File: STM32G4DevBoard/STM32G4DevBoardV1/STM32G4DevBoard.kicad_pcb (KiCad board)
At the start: 4 copper layers, 44.7 x 23.5 mm, 26 parts, among them J1 USB_B_Micro, J2 Conn_01x13, J3 Conn_01x13, U1 STM32G431KBTx, U2 LD3985M33R_SOT23, Y1 24MHz

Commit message: Finished Crystal Layout
Made changes for crystal layout
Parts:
- C180, C3: moved to F.Cu
- moved C1 31.1 mm to (112.4, 98.0), turned to 180 degrees
- moved R1 10.6 mm to (143.3, 98.2), turned to 180 degrees
- moved C180 5.99 mm to (139.2, 94.7), turned to 270 degrees
- moved C3 4.33 mm to (139.2, 91.2), turned to 270 degrees
- moved C7 3.23 mm to (136.7, 95.1)
- moved C4 3.07 mm to (131.3, 87.1)
- moved C5 2.87 mm to (131.3, 85.3)
- moved FB1 1.75 mm to (127.8, 85.3), turned to 0 degrees
- moved Y1 1.27 mm to (142.2, 93.2)
- moved RST_SW1 0.92 mm to (112.0, 98.0)
- moved C11 0.51 mm to (122.4, 91.8)
- moved C6 0.51 mm to (124.4, 91.8)
- moved C8 0.51 mm to (126.3, 91.8)
- moved C10 0.25 mm to (116.6, 91.6)
- moved C12 0.25 mm to (118.7, 95.8)
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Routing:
- net GND: track 0.00 -> 38.3 mm, vias 0 -> 15
- net OSC_IN: track 0.00 -> 8.04 mm
- net OSC_OUT: track 0.00 -> 4.94 mm

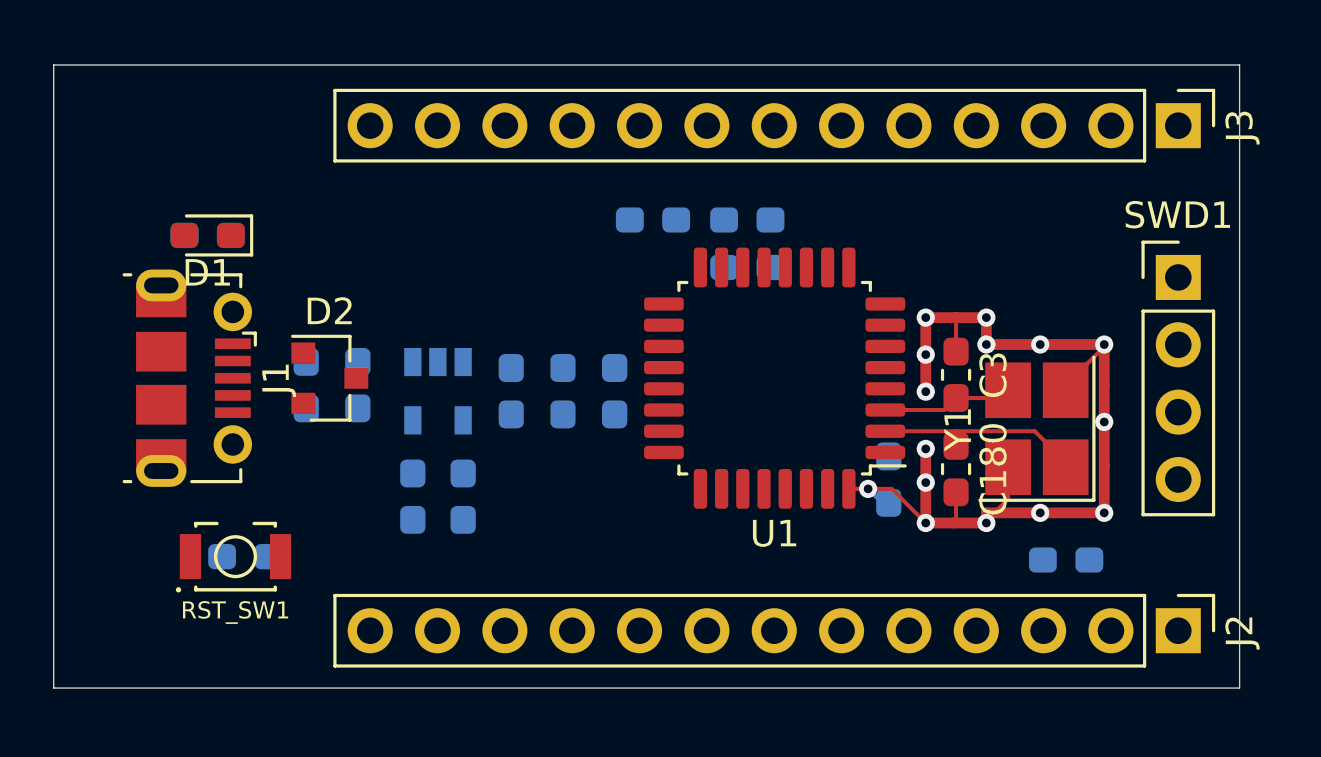
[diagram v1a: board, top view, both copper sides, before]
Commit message: Made plenty of Progress, finish routing power and a couple of pins
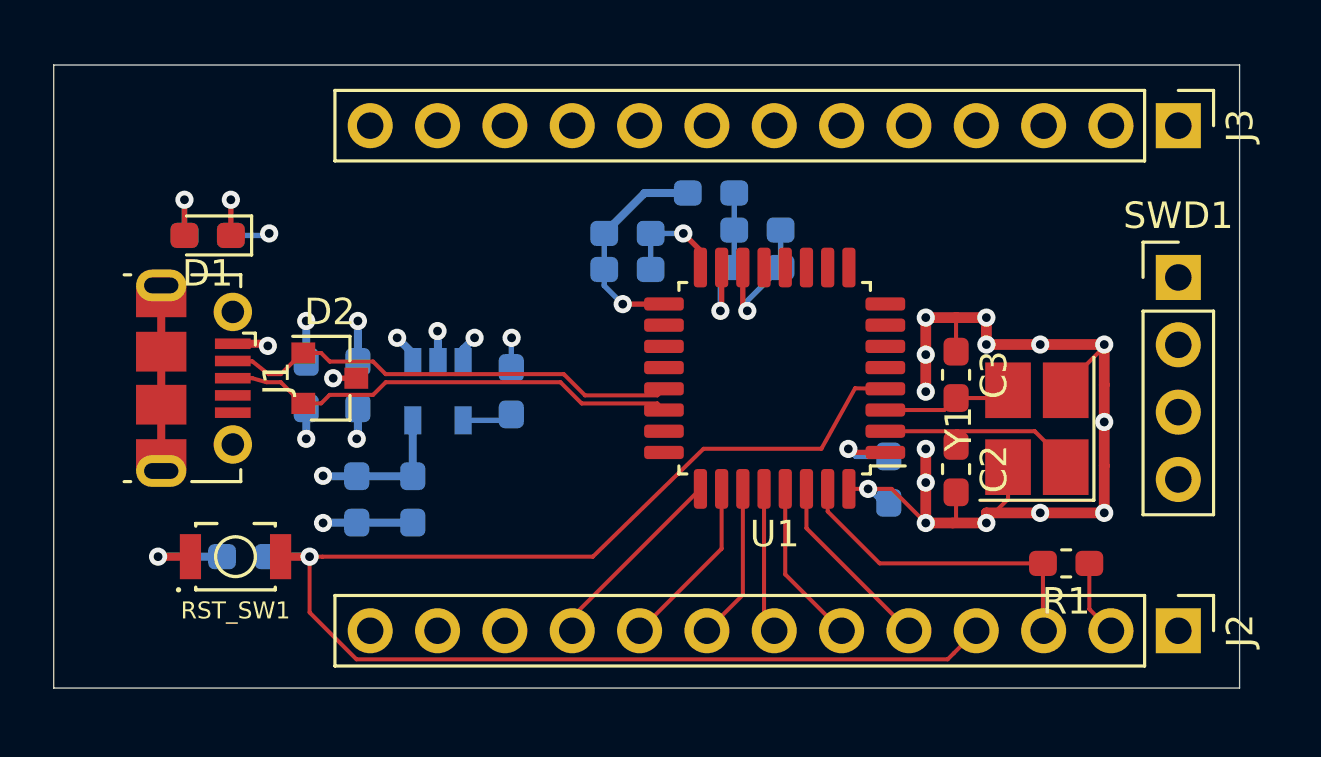
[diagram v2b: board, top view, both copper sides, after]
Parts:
- R1: moved to F.Cu
- moved C6 6.43 mm to (126.8, 85.9), turned to 180 degrees
- moved C8 4.62 mm to (126.8, 87.2), turned to 180 degrees
- moved C13 4.02 mm to (116.6, 95.9)
- moved FB1 2.41 mm to (129.9, 84.3)
- moved C5 0.54 mm to (131.7, 85.7)
- moved C4 0.38 mm to (131.7, 87.1)
- moved R1 0.13 mm to (143.3, 98.3)
- moved C12 0.10 mm to (118.7, 95.9)
- renumbered C180 to C2
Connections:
- C8 pad 1: 3.3V_VDD -> GND
- C8 pad 2: GND -> 3.3V_VDD
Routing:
- net NRST: track 0.00 -> 55.8 mm, vias 0 -> 1
- net GND: track 38.3 -> 71.0 mm, vias 15 -> 25
- net USB_D-: track 0.00 -> 17.5 mm
- net USB_D+: track 0.00 -> 17.4 mm
- net 3.3V_VDD: track 0.00 -> 16.8 mm, vias 0 -> 3
- net BOOT0: track 0.00 -> 12.3 mm
- net 5V_USB: track 0.00 -> 8.19 mm, vias 0 -> 6
- net PA15: track 0.00 -> 7.35 mm
- net PB7: track 0.00 -> 6.95 mm
- net PB3: track 0.00 -> 6.63 mm
- net 3.3V_VDDA: track 0.00 -> 6.32 mm, vias 0 -> 1
- net PB6: track 0.00 -> 6.23 mm
- net PB4: track 0.00 -> 5.91 mm
- net PB5: track 0.00 -> 5.51 mm
- net Net-(D1-Pad2): track 0.00 -> 2.99 mm, vias 0 -> 1
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- added copper zone on PWR, net 5V_USB

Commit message: Finish Power splitting and pin routing
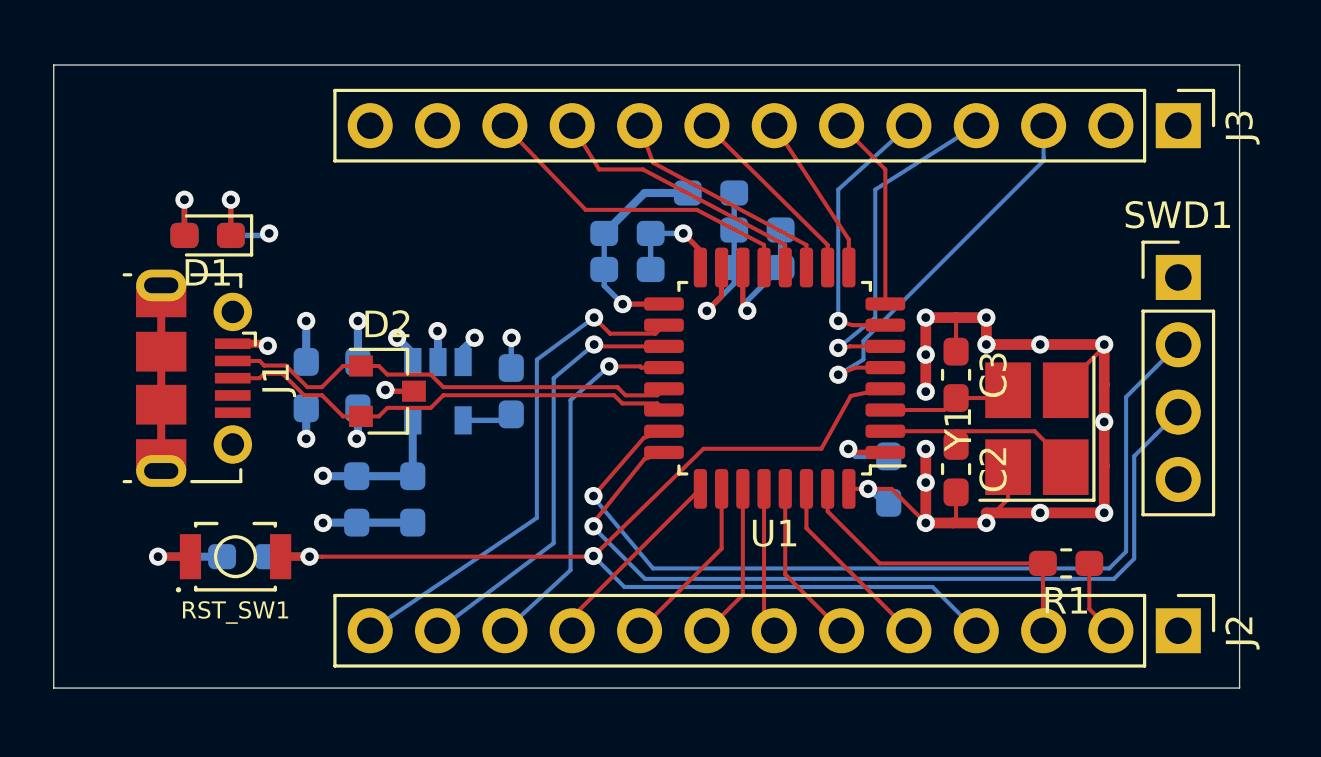
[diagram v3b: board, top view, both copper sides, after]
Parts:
- moved D2 2.23 mm to (117.7, 91.8)
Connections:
- net SWCLK renamed SWCLK_P
- net SWDIO renamed SWDIO_M
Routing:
- net SWDIO_M: track 0.00 -> 34.0 mm, vias 0 -> 1
- net SWCLK_P: track 0.00 -> 31.8 mm, vias 0 -> 1
- net PA8: track 0.00 -> 19.3 mm, vias 0 -> 1
- net PA9: track 0.00 -> 16.4 mm, vias 0 -> 1
- net Net-(J3-Pad3): track 0.00 -> 14.6 mm, vias 0 -> 1
- net PA10: track 0.00 -> 13.8 mm, vias 0 -> 1
- net NRST: track 55.8 -> 42.8 mm, vias 1 -> 2
- net Net-(J3-Pad4): track 0.00 -> 12.9 mm, vias 0 -> 1
- net SWO: track 0.00 -> 12.3 mm
- net Net-(J3-Pad10): track 0.00 -> 10.5 mm
- net Net-(J3-Pad5): track 0.00 -> 10.3 mm, vias 0 -> 1
- net Net-(J3-Pad9): track 0.00 -> 8.90 mm
- net Net-(J3-Pad6): track 0.00 -> 7.41 mm
- net Net-(J3-Pad8): track 0.00 -> 7.25 mm
- net Net-(J3-Pad7): track 0.00 -> 6.19 mm
- added copper zone on PWR, net 3.3V_VDDA

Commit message: Completed splitting ground plane and board routing
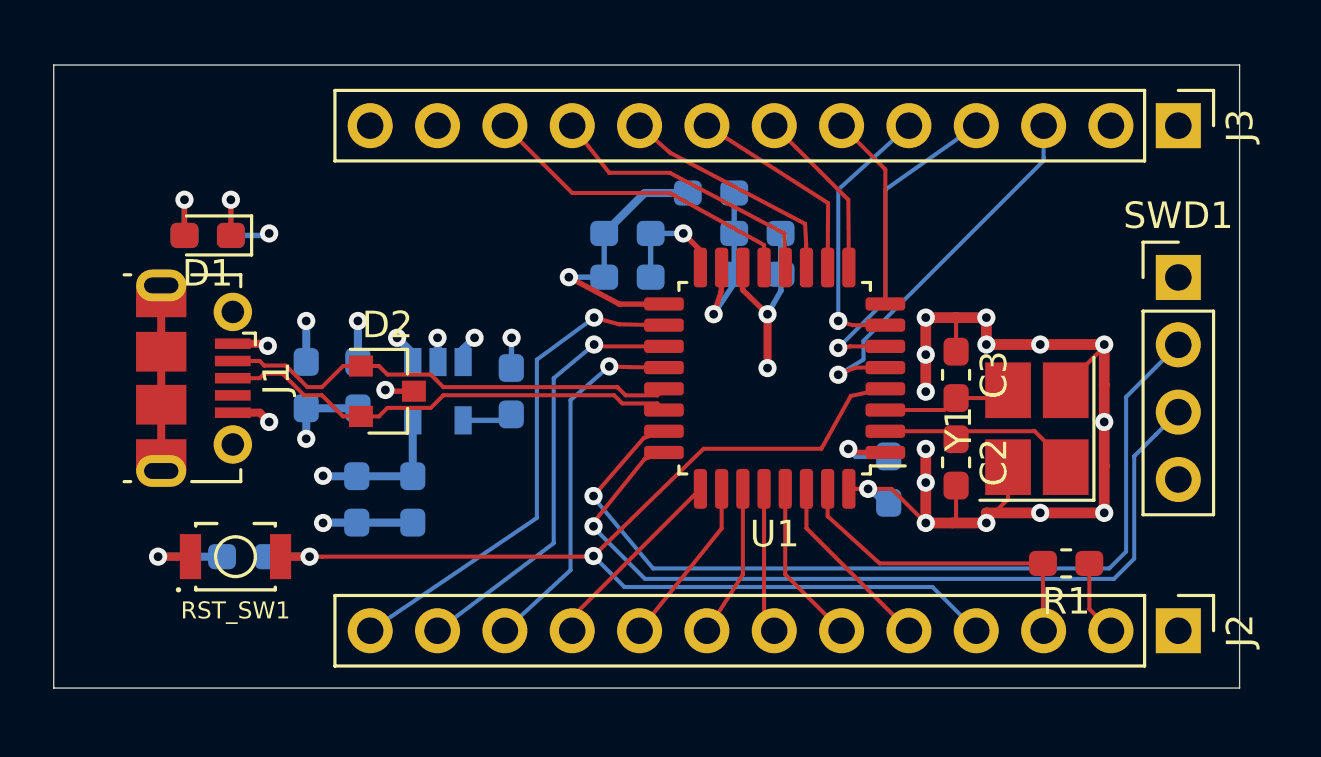
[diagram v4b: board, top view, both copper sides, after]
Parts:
- moved C8 0.29 mm to (126.8, 87.5)
- moved C2 0.25 mm to (139.2, 94.5)
- moved C4 0.25 mm to (131.7, 87.4)
- moved C5 0.13 mm to (131.7, 85.9)
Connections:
- net SWCLK_P renamed SWCLK
- net SWDIO_M renamed SWDIO
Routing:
- net GND: track 71.2 -> 75.8 mm, vias 25 -> 26
- net 3.3V_VDD: track 16.8 -> 19.1 mm
- net Net-(J3-Pad8): track 7.25 -> 7.85 mm

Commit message: Updated Silkscreen label for pins
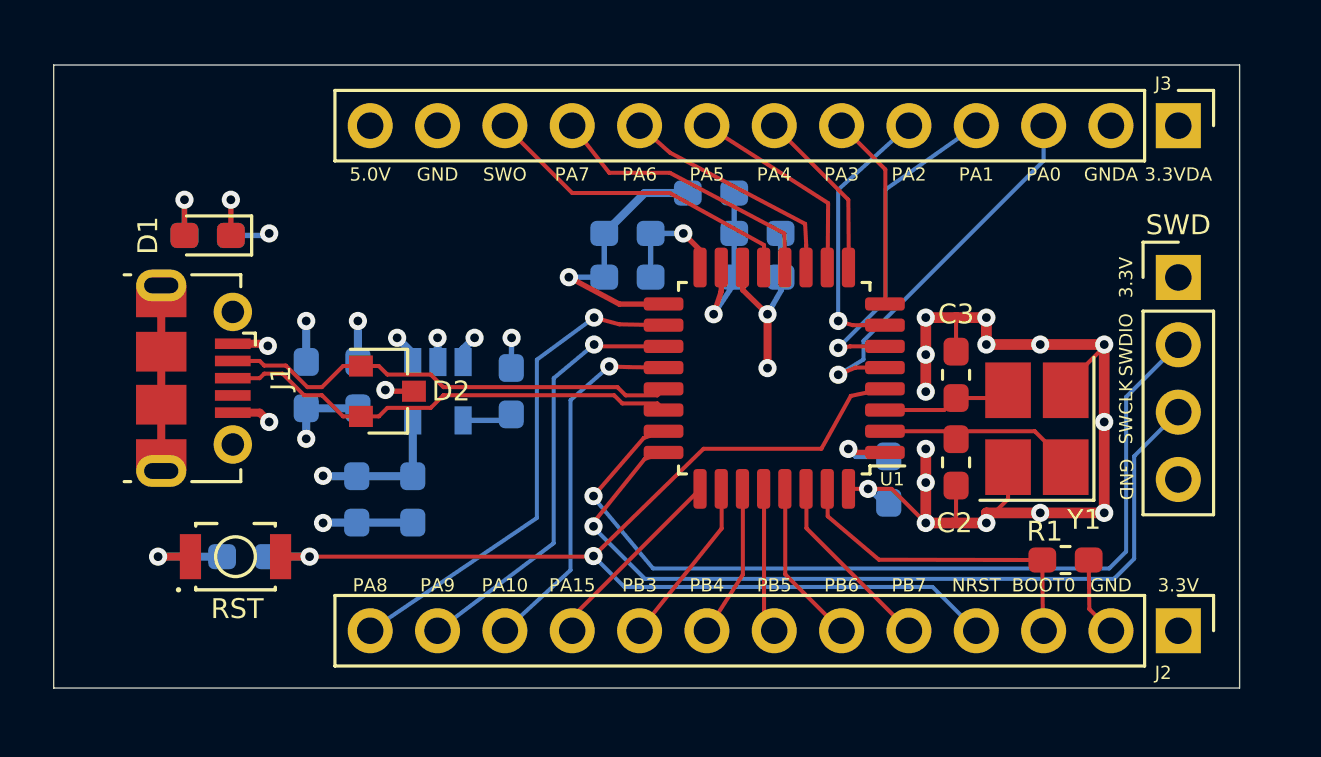
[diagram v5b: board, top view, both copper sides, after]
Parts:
- moved R1 0.13 mm to (143.3, 98.2)
- moved C4 0.11 mm to (131.7, 87.5)
- renumbered RST_SW1 to RST, SWD1 to SWD
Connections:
- net Net-(J3-Pad10) renamed PA7
- net Net-(J3-Pad3) renamed PA0
- net Net-(J3-Pad4) renamed PA1
- net Net-(J3-Pad5) renamed PA2
- net Net-(J3-Pad6) renamed PA3
- net Net-(J3-Pad7) renamed PA4
- net Net-(J3-Pad8) renamed PA5
- net Net-(J3-Pad9) renamed PA6
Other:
- board text added: "3.3V"
- board text added: "3.3VDA"
- board text added: "5.0V"
- board text added: "BG STM32 BRK V1.00"
- board text added: "BOOT0"
- board text added: "GND"
- board text added: "GNDA"
- board text added: "NRST"
- board text added: "PA0"
- board text added: "PA1"
- board text added: "PA10"
- board text added: "PA15"
- board text added: "PA2"
- board text added: "PA3"
- board text added: "PA4"
- board text added: "PA5"
- board text added: "PA6"
- board text added: "PA7"
- board text added: "PA8"
- board text added: "PA9"
- board text added: "PB3"
- board text added: "PB4"
- board text added: "PB5"
- board text added: "PB6"
- board text added: "PB7"
- board text added: "SWCLK"
- board text added: "SWDIO"
- board text added: "SWO"

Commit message: Added Ferride Beads and test LED
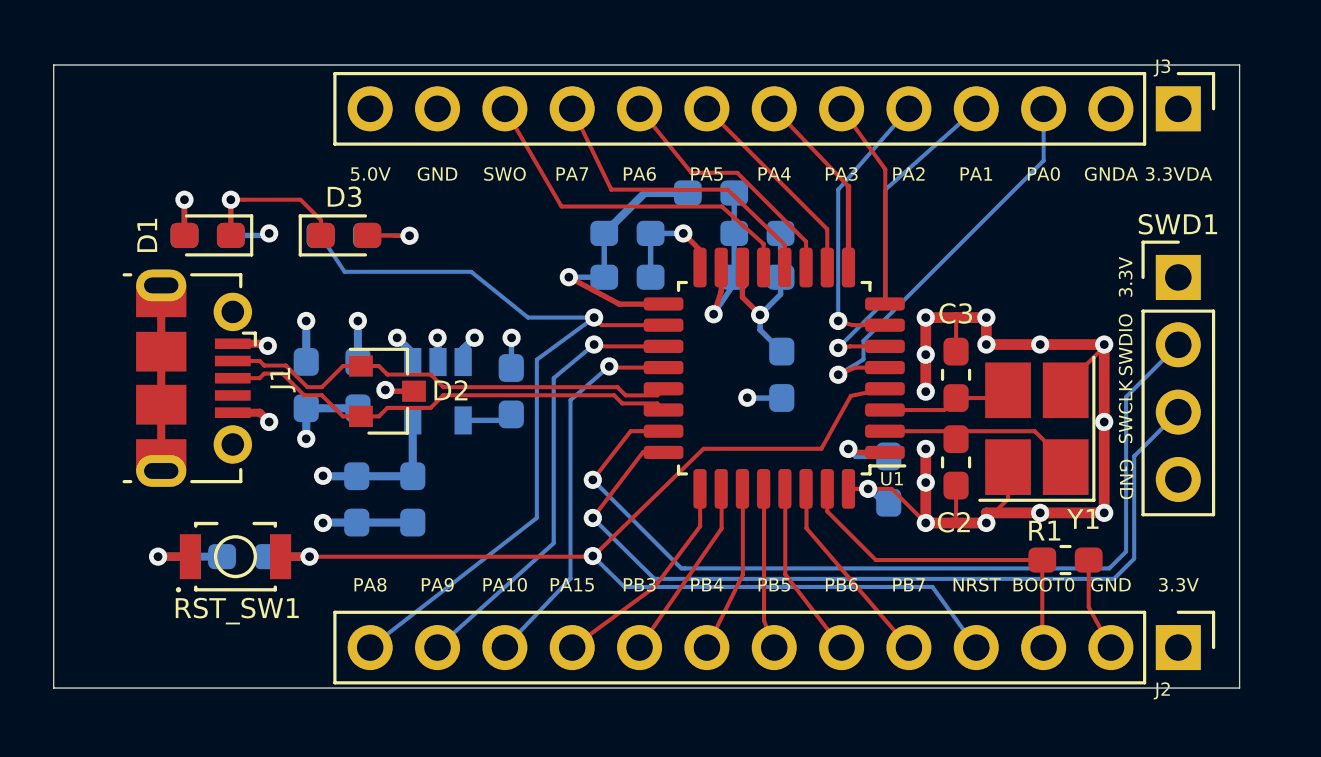
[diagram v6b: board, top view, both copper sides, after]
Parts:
- added D3: LED, LED_SMD:LED_0603_1608Metric_Pad1.05x0.95mm_HandSolder, F.Cu at (116.1, 85.9)
- added FB2: 600R@100MHz, Inductor_SMD:L_0603_1608Metric_Pad1.05x0.95mm_HandSolder, B.Cu at (132.6, 91.2)
- added R3: 100, Resistor_SMD:R_0603_1608Metric_Pad1.05x0.95mm_HandSolder, B.Cu at (116.1, 85.9)
- R2: value 3K -> 330
- moved J2 0.64 mm to (147.6, 101.5)
- moved J3 0.63 mm to (147.6, 81.2)
- renumbered RST to RST_SW1, SWD to SWD1
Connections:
- C4 pad 2: GND -> GNDA
- C5 pad 2: GND -> GNDA
- J3 pad 2: GND -> GNDA
- U1 pad 14: GND -> GNDA
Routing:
- net PA8: track 18.9 -> 31.0 mm
- net GNDA: track 0.00 -> 7.18 mm, vias 0 -> 1
- net Net-(D3-Pad2): track 0.00 -> 3.20 mm, vias 0 -> 1
- net GND: track 75.9 -> 74.5 mm, vias 26 -> 25
- net SWO: track 12.2 -> 13.3 mm
- net PA7: track 10.7 -> 11.6 mm
- net PA15: track 7.35 -> 8.13 mm
- net BOOT0: track 12.4 -> 13.0 mm
- net PA0: track 14.6 -> 15.2 mm
- net PA4: track 6.51 -> 7.11 mm
- net PB4: track 5.75 -> 6.30 mm
- net PB5: track 5.51 -> 6.06 mm
- net PA10: track 13.8 -> 14.3 mm
- net PB3: track 6.44 -> 6.95 mm
- net NRST: track 42.8 -> 43.3 mm
- added copper zone on GND, net GNDA

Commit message: Last minute tweak, adjustment
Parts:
- moved FB2 0.82 mm to (131.8, 91.1)
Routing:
- net PA8: track 31.0 -> 30.4 mm
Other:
- board size 44.7 x 23.5 mm -> 43.1 x 23.9 mm
